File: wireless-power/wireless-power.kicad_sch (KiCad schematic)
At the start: 6 parts, among them U1 TPS62112RSAR

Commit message: transistor
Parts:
- added Q1: BD139, SOT-32_STM, symbol BD139:BD139
- added U2: NE555DR, D8, symbol ul_NE555DR:NE555DR
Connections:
- net GND: now also Q1.3, U2.1 (GND)

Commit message: imported schematic
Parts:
- added C4: 40pF, wireless-power-footprints:CAPC0603X33N, symbol GRM0335C1H390JA01D:GRM0335C1H390JA01D
- added C5: 10nF, wireless-power-footprints:G-155_MUR, symbol GRM155R71C103KA01D:GRM155R71C103KA01D
- added C6: 100nF, wireless-power-footprints:G-033_MUR, symbol GRM033R60J104KE19D:GRM033R60J104KE19D
- added J1, J2: Screw_Terminal_01x01, TestPoint:TestPoint_Keystone_5019_Minature, symbol Connector:Screw_Terminal_01x01
- added R2: 120, wireless-power-footprints:RC0603N_PAN, symbol ERA_3AEB121V:ERA-3AEB121V
- added R3: 18k, wireless-power-footprints:RC0603N_YAG, symbol RC0603JR_0718KL:RC0603JR-0718KL
- added R4: 20k, wireless-power-footprints:RC0402N_YAG, symbol RC0402FR_0720KL:RC0402FR-0720KL
- C1: footprint TMK212B7105KG-T:CAPC2012X135N -> wireless-power-footprints:CAPC2012X135N
- C2, C3: footprint CAP_C3225-250_TDK -> wireless-power-footprints:CAP_C3225-250_TDK
- L1: footprint DR125 -> wireless-power-footprints:DR125
- Q1: footprint SOT-32_STM -> wireless-power-footprints:SOT-32_STM
- R1: footprint RC0603N_YAG -> wireless-power-footprints:RC0603N_YAG
- U1: footprint TPS62112RSAR:QFN65P400X400X100-17N -> wireless-power-footprints:QFN65P400X400X100-17N
- U2: footprint D8 -> wireless-power-footprints:D8
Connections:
- net +5V: now also U2.4 (RESET), U2.8 (VCC), C6.1, R3.1
- net +9V: now also J1.1 (Pin_1)
- net GND: now also C4.2, C5.2, J2.1 (Pin_1)
- net at U2.2 (TRIG): now also U2.6 (THRES), C4.1, R4.2
- net at U2.3 (OUT): now also R2.1
- net at U2.5 (CONT): now also C5.1
- net at U2.7 (DISCH): now also R3.2, R4.1
- net at Q1.1: now also R2.2
- net Coil_Low: now reaches Q1.2
- net Coil_Low: now also C6.2
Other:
- moved on the sheet: Q1, U2

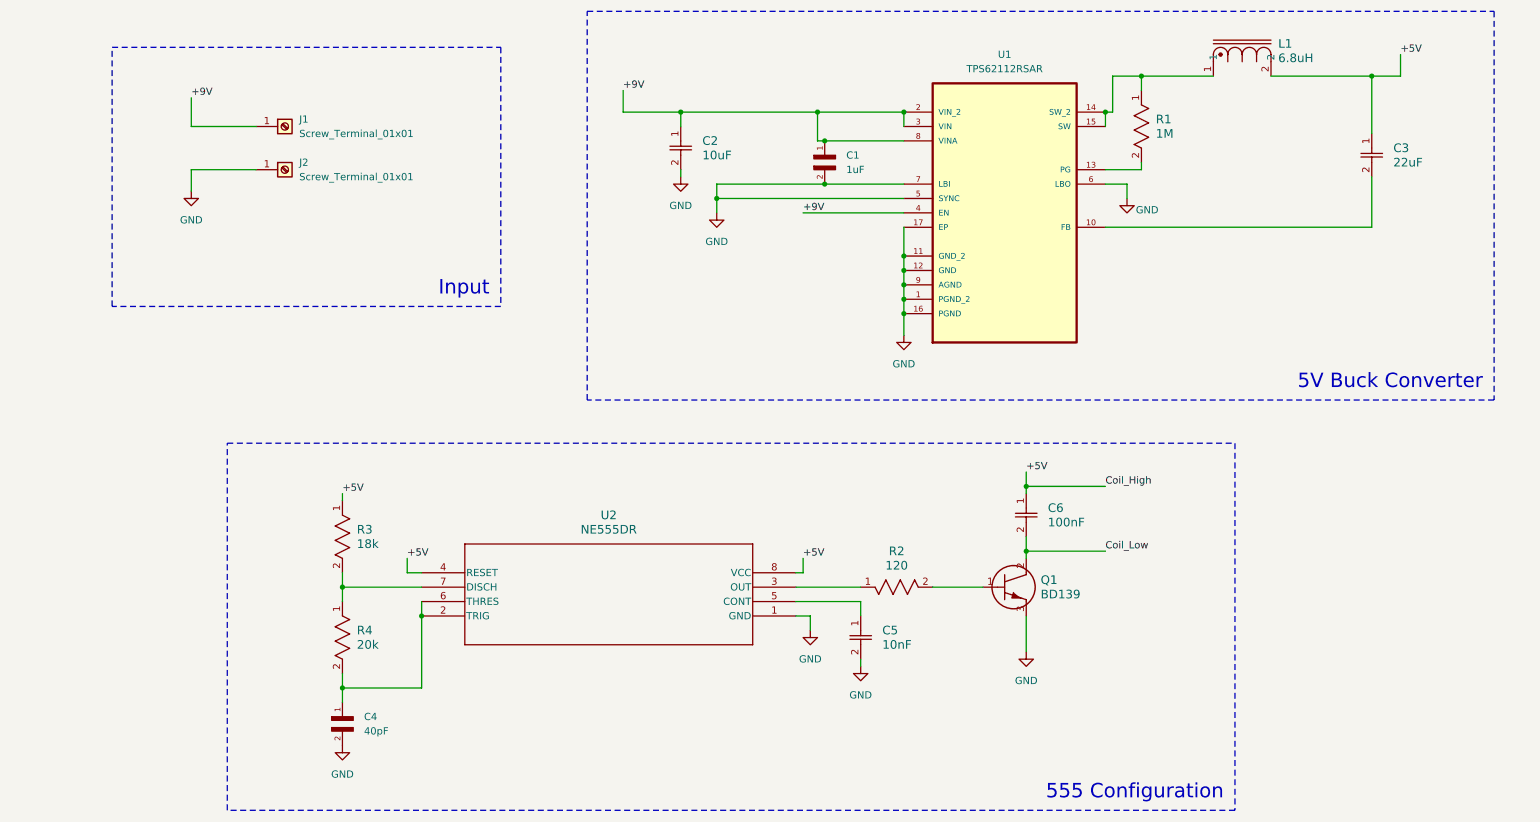
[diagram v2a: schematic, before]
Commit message: preliminary layout
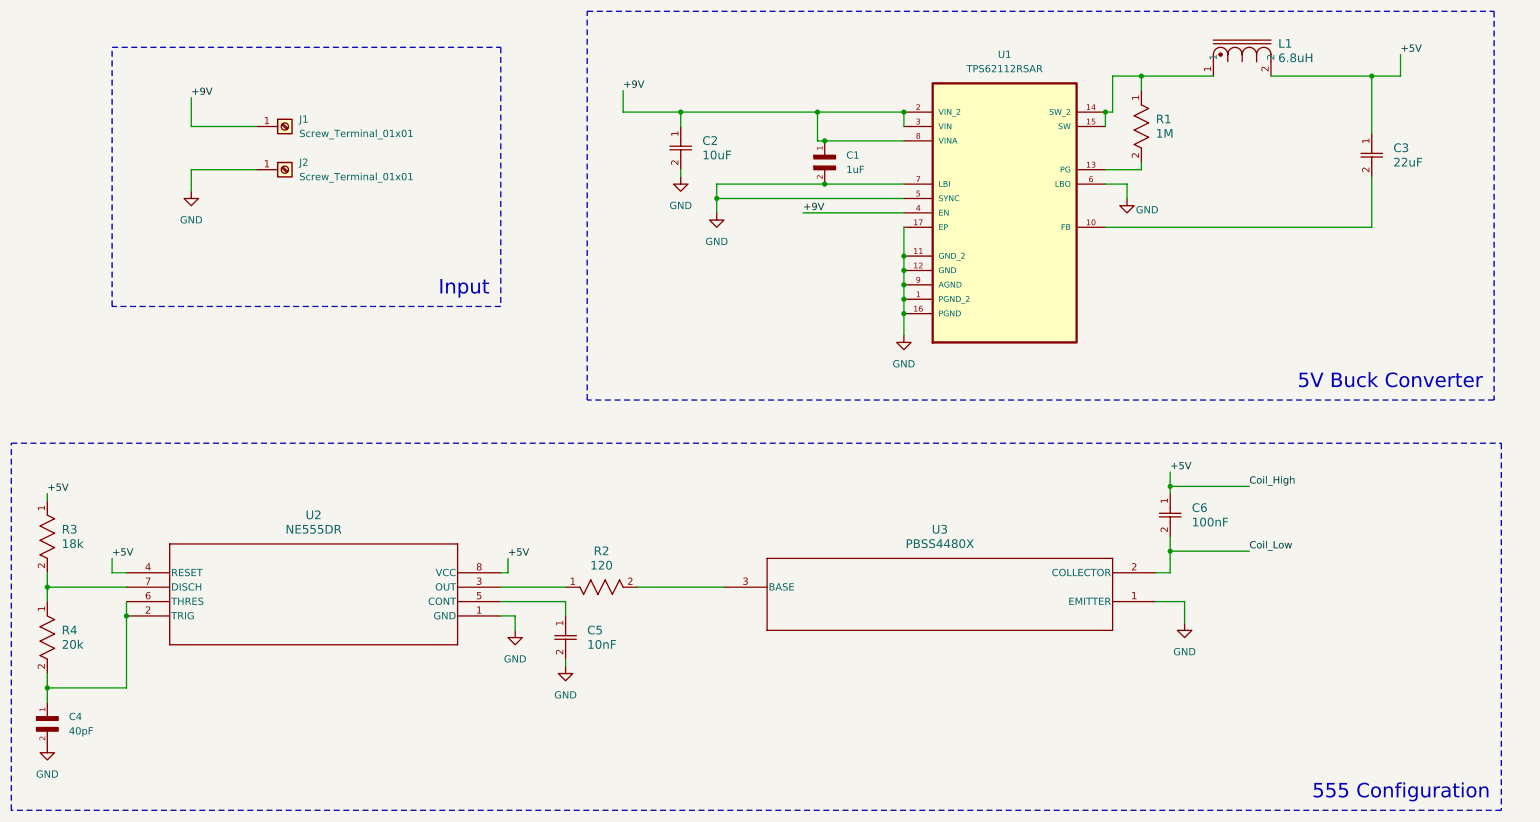
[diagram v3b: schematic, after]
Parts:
- removed Q1: BD139, wireless-power-footprints:SOT-32_STM, symbol BD139:BD139
- added U3: PBSS4480X, wireless-power-footprints:SOT89_NXP, symbol ul_PBSS4480X:PBSS4480X
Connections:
- net Coil_Low: now also U3.2 (COLLECTOR)
- net GND: now also U3.1 (EMITTER)
- net at R2.2: now also U3.3 (BASE)
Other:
- moved on the sheet: C4, C5, C6, R2, R3, R4, U2

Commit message: changed coil terminal
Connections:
- net Coil_Low is gone; now on net +5V: C6.2, U3.2 (COLLECTOR)
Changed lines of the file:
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@@
+	(wire
+		(pts
+			(xy 234.95 101.6) (xy 234.95 113.03)
+		)
+		(stroke
+			(width 0)
+			(type default)
+		)
+	)
 	(wire
 		(pts
@@
 		)
 	)
-	(label "Coil_Low"
-		(at 234.95 113.03 0)
-		(fields_autoplaced yes)
-		(effects
-			(font
-				(size 1.27 1.27)
-			)
-			(justify left bottom)
-		)
-	)
 	(label "+5V"
 		(at 22.86 102.87 0)
 		(fields_autoplaced yes)
 		(effects
-			(font
-				(size 1.27 1.27)
-			)
-			(justify left bottom)
-		)
-	)
-	(label "Coil_High"
-		(at 234.95 101.6 0)
-		(fields_autoplaced yes)
-		(effects

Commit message: finalized transmitter PCB
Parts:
- removed C4: 40pF, wireless-power-footprints:CAPC0603X33N, symbol GRM0335C1H390JA01D:GRM0335C1H390JA01D
- added C4: 39pF, CAPC6333_33N_KEM, symbol C0201C390J3GACTU:C0201C390J3GACTU
- added TP1, TP2, TP3, TP4: TestPoint, TestPoint:TestPoint_THTPad_1.0x1.0mm_Drill0.5mm, symbol Connector:TestPoint
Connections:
- net +5V: now also TP1.1, TP2.1, TP3.1
- net GND: now also C4.2, TP4.1
- net at R4.2, U2.2 (TRIG), U2.6 (THRES): now also C4.1

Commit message: updated buck converter
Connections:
- net +5V: now also U1.10 (FB)
- net GND: now also C3.2
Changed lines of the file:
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@@
+	)
+	(junction
+		(at 250.19 29.21)
+		(diameter 0)
+		(color 0 0 0 0)
 	)
 	(junction
@@
 	(wire
 		(pts
+			(xy 250.19 55.88) (xy 250.19 29.21)
+		)
+		(stroke
+			(width 0)
+			(type default)
+		)
+	)
+	(wire
+		(pts
 			(xy 59.69 45.72) (xy 48.26 45.72)
 		)
@@
 	(wire
 		(pts
+			(xy 250.19 29.21) (xy 238.76 29.21)
+		)
+		(stroke
+			(width 0)
+			(type default)
+		)
+	)
+	(wire
+		(pts
 			(xy 215.9 29.21) (xy 228.6 29.21)
 		)
@@
 	(wire
 		(pts
-			(xy 209.55 55.88) (xy 256.54 55.88)
-		)
-		(stroke
-			(width 0)
-			(type default)
-		)
-	)
-	(wire
-		(pts
 			(xy 36.83 119.38) (xy 22.86 119.38)
 		)
@@
 	(wire
 		(pts
-			(xy 256.54 29.21) (xy 238.76 29.21)
+			(xy 256.54 29.21) (xy 250.19 29.21)
 		)
 		(stroke
@@
 		(pts
 			(xy 173.99 68.58) (xy 173.99 71.12)
+		)
+		(stroke
+			(width 0)
+			(type default)
+		)
+	)
+	(wire
+		(pts
+			(xy 209.55 55.88) (xy 250.19 55.88)
 		)
 		(stroke
@@
 					(unit 1)
 				)
+			)
+		)
+	)
+	(symbol
+		(lib_id "power:GND")
+		(at 256.54 55.88 0)
+		(unit 1)
+		(exclude_from_sim no)
+		(in_bom yes)
+		(on_board yes)
+		(dnp no)
+		(property "Reference" "#PWR010"
+			(at 256.54 62.23 0)
+			(effects
+				(font
+					(size 1.27 1.27)
+				)
+				(hide yes)
+			)
+		)
+		(property "Value" "GND"
+			(at 260.096 57.912 0)
+			(effects
+				(font
+					(size 1.27 1.27)
+				)
+			)
+		)
+		(property "Footprint" ""
+			(at 256.54 55.88 0)
+			(effects
+				(font
+					(size 1.27 1.27)
+				)
+				(hide yes)
+			)
+		)
+		(property "Datasheet" ""
+			(at 256.54 55.88 0)
+			(effects
+				(font
+					(size 1.27 1.27)
+				)
+				(hide yes)
+			)
+		)
+		(property "Description" "Power symbol creates a global label with name \"GND\" , ground"
+			(at 256.54 55.88 0)
+			(effects
+				(font
+					(size 1.27 1.27)
+				)
+				(hide yes)
+			)
+		)
+		(pin "1"
+		)
+		(instances
+			(project "wireless-power"
+				(path "/f75fbfb2-d47e-4bc2-9c6f-9018bbdc426d"
+					(reference "#PWR010")
+					(unit 1)
+				)
